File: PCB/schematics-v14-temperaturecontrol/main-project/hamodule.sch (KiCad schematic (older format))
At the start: 60 parts, among them J1 2604-1104, J10 GND 3.3V, J11 Current Jumper, J2 ESP Relays, J3 2604-1102, J4 2604-1104, J5 Conn_01x02, J6 ESP Sensors, J9 Current Jumper, K1 PCN-105D, K2 PCN-105D, K3 PCN-105D, K4 PCN-105D, U1 ULN2003A, U2 LD1117AV33_TO220, U3 HCPL3700, U4 HCPL3700, U5 HCPL3700, U6 HCPL3700

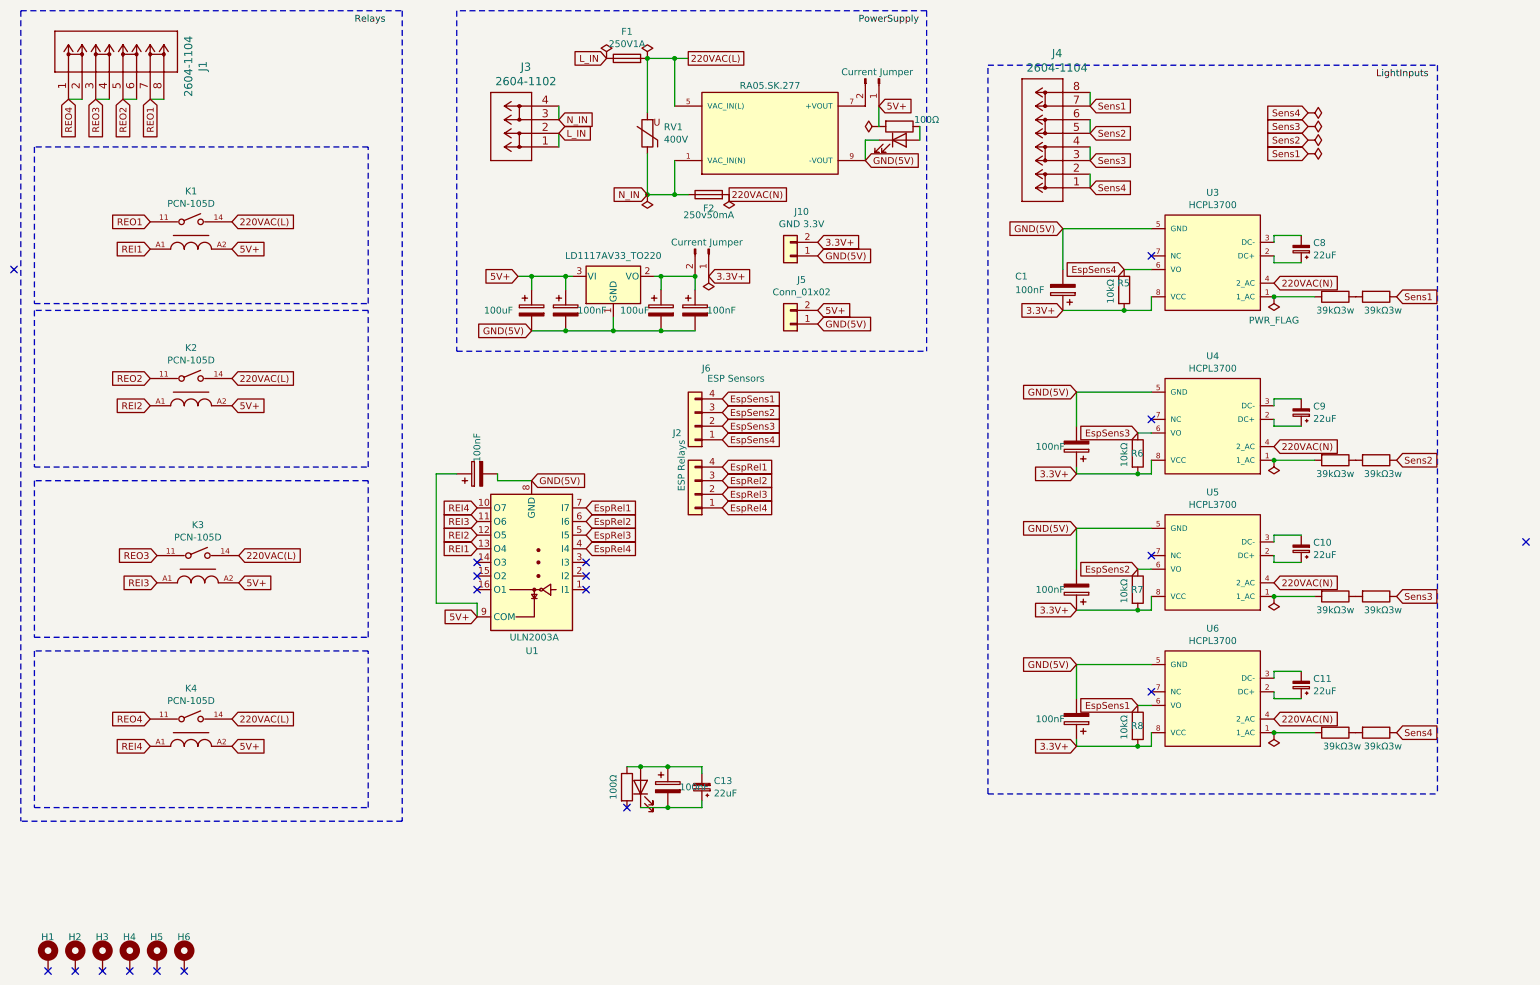
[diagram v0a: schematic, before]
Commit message: half way with new optocouplers
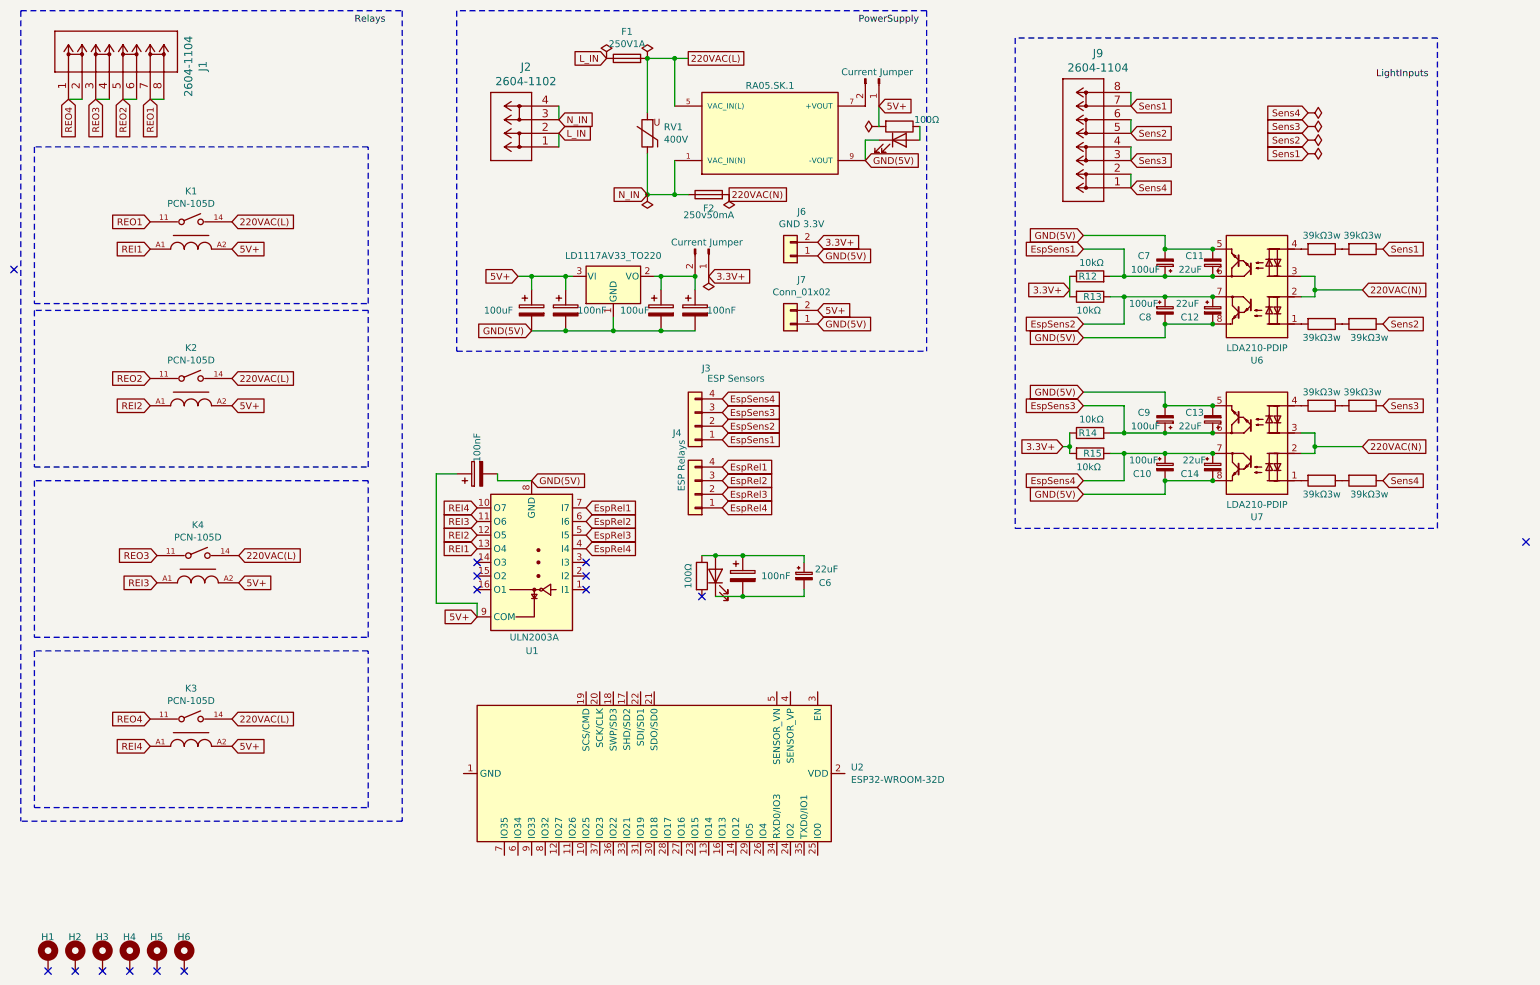
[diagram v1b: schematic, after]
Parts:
- removed C1, C2, C3, C4: 100nF, Capacitor_SMD:C_0805_2012Metric_Pad1.15x1.40mm_HandSolder, symbol Device:CP
- removed C11: 22uF, Capacitor_Tantalum_SMD:CP_EIA-3528-21_Kemet-B_Pad1.50x2.35mm_HandSolder, symbol Device:CP_Small
- removed R10, R12, R17: 39kΩ3w, Resistor_SMD:R_2512_6332Metric_Pad1.52x3.35mm_HandSolder, symbol Device:R
- removed R7, R8: 10kΩ, Resistor_SMD:R_1206_3216Metric_Pad1.42x1.75mm_HandSolder, symbol Device:R
- removed U3, U4, U5, U6: HCPL3700, Package_DIP:DIP-8_W7.62mm_Socket_LongPads, symbol HCPL-3700-000:HCPL3700
- added C13, C14: 22uF, Capacitor_Tantalum_SMD:CP_EIA-3528-21_Kemet-B_Pad1.50x2.35mm_HandSolder, symbol Device:CP_Small
- added C7, C8, C9: 100uF, Capacitor_SMD:C_0805_2012Metric_Pad1.15x1.40mm_HandSolder, symbol Device:CP_Small
- added R14: 10kΩ, Resistor_SMD:R_1206_3216Metric_Pad1.42x1.75mm_HandSolder, symbol Device:R
- added R18, R19, R22, R23: 39kΩ3w, Resistor_SMD:R_2512_6332Metric_Pad1.52x3.35mm_HandSolder, symbol Device:R
- added U2: ESP32-WROOM-32D, RF_Module:ESP32-WROOM-32, symbol RF_Module:ESP32-WROOM-32D
- added U6, U7: LDA210-PDIP, Package_DIP:DIP-8_W7.62mm_Socket_LongPads, symbol LDA210-PDIP:LDA210-PDIP
- C10: value 22uF -> 100uF; footprint Capacitor_Tantalum_SMD:CP_EIA-3528-21_Kemet-B_Pad1.50x2.35mm_HandSolder -> Capacitor_SMD:C_0805_2012Metric_Pad1.15x1.40mm_HandSolder; JLCPCB C110051 -> C28233
- R15: value 39kΩ3w -> 10kΩ; footprint Resistor_SMD:R_2512_6332Metric_Pad1.52x3.35mm_HandSolder -> Resistor_SMD:R_1206_3216Metric_Pad1.42x1.75mm_HandSolder; JLCPCB C144424 -> C17902
- renumbered C6 to C1, C8 to C11, C9 to C12, C7 to C2, C5 to C3, C12 to C5, C13 to C6, D9 to D2, J3 to J2, J6 to J3, J2 to J4, J11 to J5, J10 to J6, J5 to J7, J9 to J8, J4 to J9, K4 to K3, K3 to K4, R9 to R11, R5 to R12, R6 to R13, R14 to R17, R11 to R20, R13 to R21, R1 to R9, RA05.SK.277 to RA05.SK.1, U2 to U4
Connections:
- net 220VAC(N): now also U6.2, U6.3, U7.2, U7.3
- net 3.3V+: now also R12.1, R15.2, R14.1; no longer R12.2
- net EspSens1: now also C11.1, J3.1 (Pin_1), R12.2, C7.1, U6.6; no longer J3.4 (Pin_4)
- net EspSens2: now also C12.1, J3.2 (Pin_2), R13.1, C8.1, U6.7; no longer J3.3 (Pin_3)
- net EspSens3: now also J3.3 (Pin_3), C13.1, C9.1, R14.2, U7.6; no longer J3.2 (Pin_2), R13.1
- net EspSens4: now also C10.1, J3.4 (Pin_4), R15.1, C14.1, U7.7; no longer J3.1 (Pin_1), R12.1
- net GND(5V): now also C10.2, C11.2, C12.2, C13.2, C14.2, C7.2, C8.2, C9.2, U6.5, U6.8, U7.5, U7.8
- net Sens3: now also R22.1; no longer R15.1
- net Sens4: now also R23.1
- net at R17.2: now also U6.1
- net at R16.2: now also U6.4
- net at C5.2, D1.1 (K): now also C6.2; no longer C6.1
- net at C5.1, D1.2 (A), R9.1: now also C6.1; no longer C6.2
- new net: R18.1, R22.2
- new net: R18.2, U7.4
- new net: R19.1, R23.2
- new net: R19.2, U7.1
- new net: U2.1 (GND), U2.15 (GND), U2.38 (GND), U2.39 (GND)
- no-connect marks 19 -> 15
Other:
- moved on the sheet: C11, C12, C6, J9, R12, R13

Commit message: removing vias
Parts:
- removed H3: MountingHole_Pad, MountingHole:MountingHole_3.2mm_M3_ISO14580_Pad, symbol Mechanical:MountingHole_Pad
- removed U2: ESP32-WROOM-32D, RF_Module:ESP32-WROOM-32, symbol RF_Module:ESP32-WROOM-32D
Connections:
- no-connect marks 15 -> 14
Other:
- moved on the sheet: C6, J3, J4
